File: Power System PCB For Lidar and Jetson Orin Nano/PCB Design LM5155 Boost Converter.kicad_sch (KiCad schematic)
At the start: 74 parts, among them J1 Conn_01x04_Pin, J2 B5B-XH-A, J5 BM06B-SRSS-TBLFSN, J6 B4B-XH-A, Q1 BSC035N04LS G, Q2 BSC035N04LS G, U1 LM5155_DSSR, U2 TPS552892RYQR

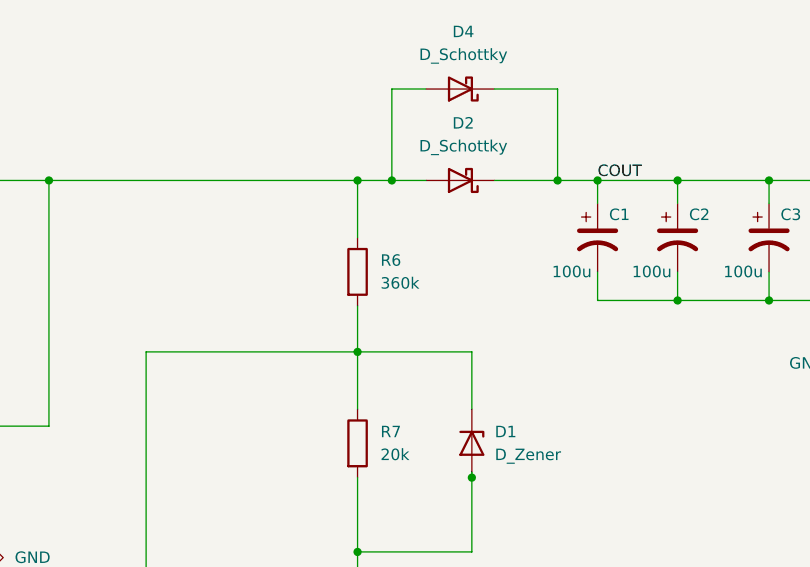
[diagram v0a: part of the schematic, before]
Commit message: adjust vias
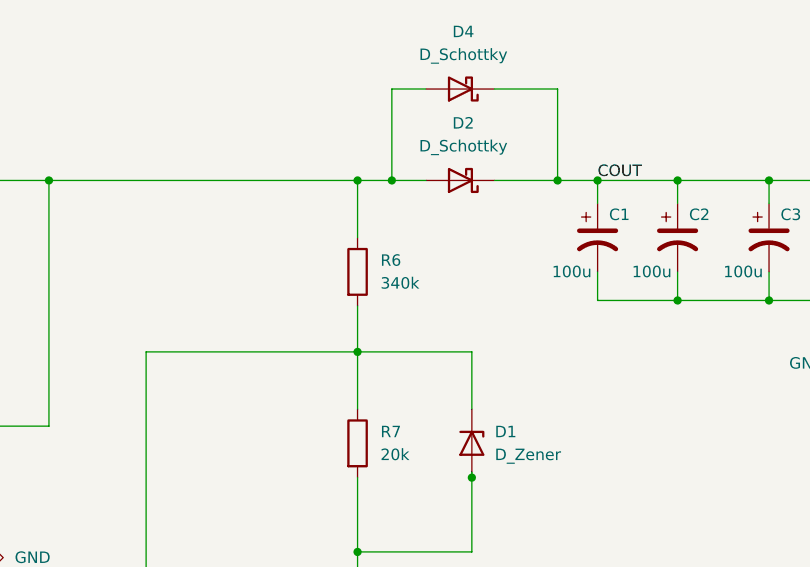
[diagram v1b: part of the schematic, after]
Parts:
- R6: value 360k -> 340k
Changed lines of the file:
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@@
 			)
 		)
-		(property "Value" "360k"
+		(property "Value" "340k"
 			(at 294.64 62.2299 0)
 			(show_name no)

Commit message: Adjust some stuff
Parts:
- added Vout6: TB002-500-02BE, 282834-2:TE_282834-2, symbol TB002-500-02BE:TB002-500-02BE
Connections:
- net GNDPWR: now also Vout6.2
- net VIN: now also Vout6.1
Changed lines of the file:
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@@
 	)
 	(junction
+		(at 68.58 55.88)
+		(diameter 0)
+		(color 0 0 0 0)
+	)
+	(junction
 		(at 347.98 50.8)
 		(diameter 0)
@@
 	)
 	(junction
+		(at 66.04 48.26)
+		(diameter 0)
+		(color 0 0 0 0)
+	)
+	(junction
 		(at 292.1 69.85)
 		(diameter 0)
@@
 	(wire
 		(pts
-			(xy 46.99 55.88) (xy 78.74 55.88)
+			(xy 46.99 55.88) (xy 68.58 55.88)
 		)
 		(stroke
@@
 	(wire
 		(pts
-			(xy 71.12 48.26) (xy 55.88 48.26)
+			(xy 71.12 48.26) (xy 66.04 48.26)
 		)
 		(stroke
@@
 	(wire
 		(pts
+			(xy 66.04 48.26) (xy 66.04 59.69)
+		)
+		(stroke
+			(width 0)
+			(type default)
+		)
+	)
+	(wire
+		(pts
 			(xy 283.21 273.05) (xy 283.21 278.13)
 		)
@@
 	(wire
 		(pts
+			(xy 66.04 48.26) (xy 55.88 48.26)
+		)
+		(stroke
+			(width 0)
+			(type default)
+		)
+	)
+	(wire
+		(pts
 			(xy 275.59 215.9) (xy 275.59 218.44)
 		)
@@
 	(wire
 		(pts
+			(xy 68.58 55.88) (xy 78.74 55.88)
+		)
+		(stroke
+			(width 0)
+			(type default)
+		)
+	)
+	(wire
+		(pts
 			(xy 425.45 63.5) (xy 425.45 66.04)
 		)
@@
 	(wire
 		(pts
+			(xy 68.58 55.88) (xy 68.58 59.69)
+		)
+		(stroke
+			(width 0)
+			(type default)
+		)
+	)
+	(wire
+		(pts
 			(xy 464.82 66.675) (xy 464.82 63.5)
 		)
@@
 					(unit 1)
 				)
+			)
+		)
+	)
+	(symbol
+		(lib_id "TB002-500-02BE:TB002-500-02BE")
+		(at 66.04 69.85 270)
+		(unit 1)
+		(body_style 1)
+		(exclude_from_sim no)
+		(in_bom yes)
+		(on_board yes)
+		(in_pos_files yes)
+		(dnp no)
+		(fields_autoplaced yes)
+		(property "Reference" "Vout6"
+			(at 72.39 68.5799 90)
+			(show_name no)
+			(do_not_autoplace no)
+			(effects
+				(font
+					(size 1.27 1.27)
+				)
+				(justify left)
+			)
+		)
+		(property "Value" "TB002-500-02BE"
+			(at 72.39 71.1199 90)
+			(show_name no)
+			(do_not_autoplace no)
+			(effects
+				(font
+					(size 1.27 1.27)
+				)
+				(justify left)
+			)
+		)
+		(property "Footprint" "282834-2:TE_282834-2"
+			(at 66.04 69.85 0)
+			(hide yes)
+			(show_name no)
+			(do_not_autoplace no)
+			(effects
+				(font
+					(size 1.27 1.27)
+				)
+				(justify bottom)
+			)
+		)
+		(property "Datasheet" ""
+			(at 66.04 69.85 0)
+			(hide yes)
+			(show_name no)
+			(do_not_autoplace no)
+			(effects
+				(font
+					(size 1.27 1.27)
+				)
+			)
+		)
+		(property "Description" ""
+			(at 66.04 69.85 0)
+			(hide yes)
+			(show_name no)
+			(do_not_autoplace no)
+			(effects
+				(font
+					(size 1.27 1.27)
+				)
+			)
+		)
+		(property "STANDARD" "Manufacturer Recommendations"
+			(at 66.04 69.85 0)
+			(hide yes)
+			(show_name no)
+			(do_not_autoplace no)
+			(effects
+				(font
+					(size 1.27 1.27)
+				)
+				(justify bottom)
+			)
+		)
+		(property "MANUFACTURER" "CUI"
+			(at 66.04 69.85 0)
+			(hide yes)
+			(show_name no)
+			(do_not_autoplace no)
+			(effects
+				(font
+					(size 1.27 1.27)
+				)
+				(justify bottom)
+			)
+		)
+		(pin "1"
+		)
+		(pin "2"
+		)
+		(instances
+			(project "PCB Design LM5155 Boost Converter"
+				(path "/085c1d8f-d12d-46a1-b7b5-945f7ea1ec15"
+					(reference "Vout6")
+					(unit 1)
+				)
